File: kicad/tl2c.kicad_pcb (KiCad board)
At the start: 4 copper layers, 120.7 x 127 mm, 92 parts, among them IC101 ATTINY20-X, P101 12VDC, P102 I2C Master, P103 Spare, P104 ISP Header, P105 LED_DRIVER, P106 240VAC, P107 LED_DRIVER, P108 LED_OUT, P301 CONN_PIR_OG, P302 CONN_PIR_EG, P303 CONN_PIR_UG, Q301 IRLML2502, Q302 IRLML2502, Q303 IRLML2502, Q401 IRLML2502, Q402 IRLML2502, Q403 IRLML2502, SW101 TL3315NF160Q, U201 LF120ABDT-TR, U202 TPS70933

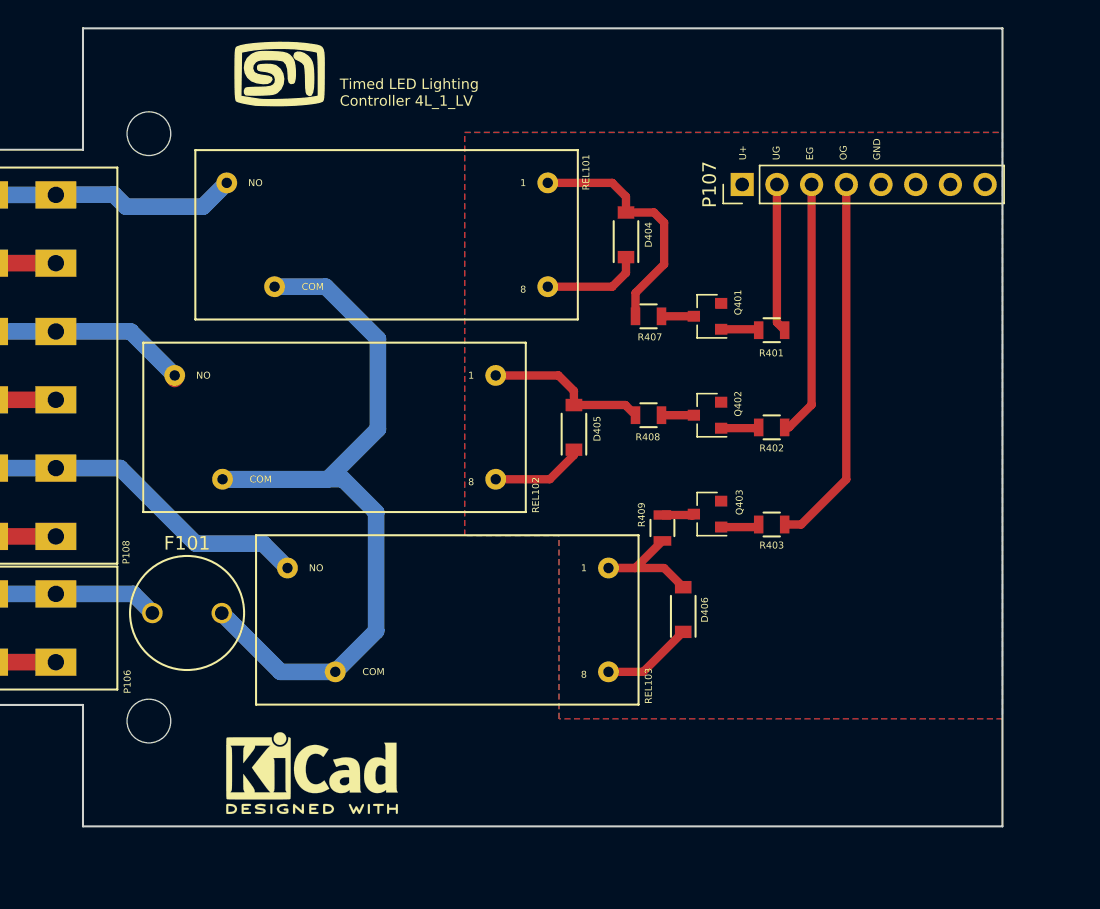
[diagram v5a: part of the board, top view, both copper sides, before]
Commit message: Created the Gerbers and submitted the order for boards and stensils
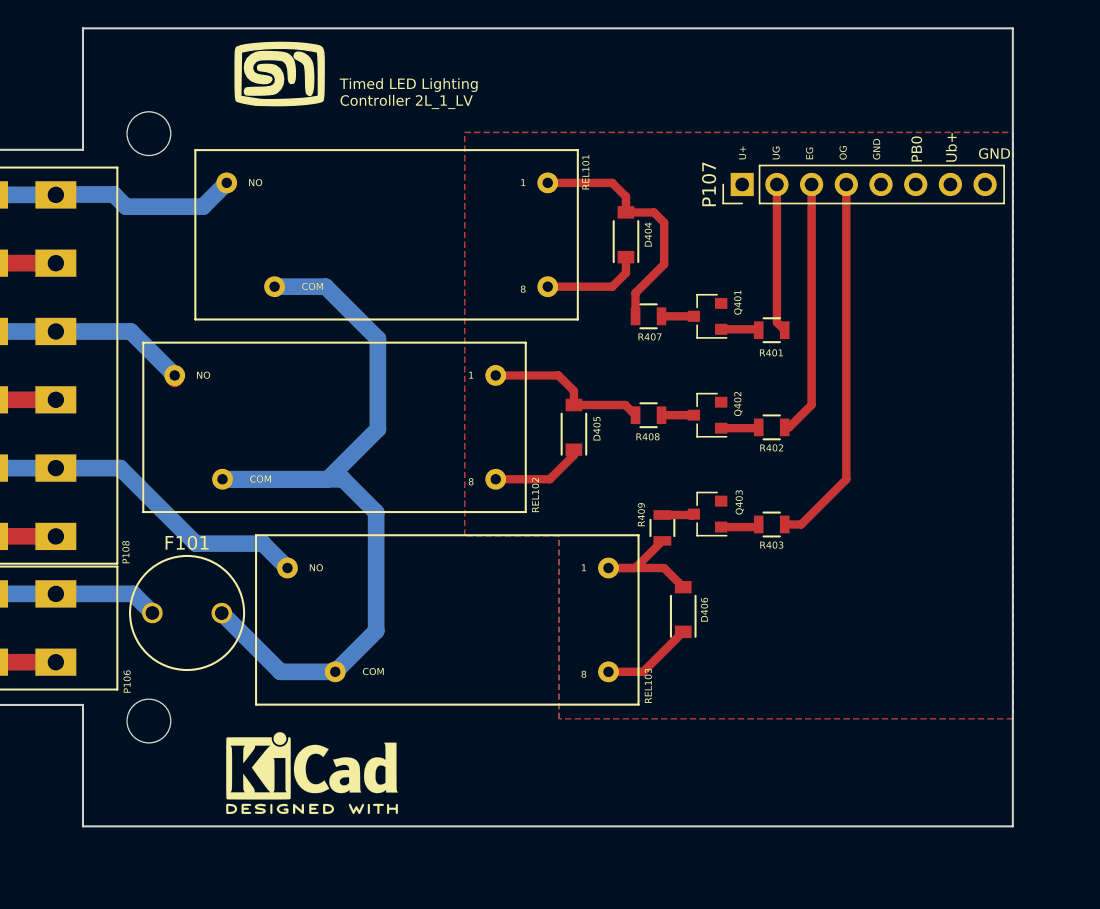
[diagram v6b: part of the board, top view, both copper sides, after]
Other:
- outline, holes or cut-outs redrawn
- board text added: "Timed LED Lighting Controller 2L_1_LV"
- board text removed: "Timed LED Lighting Controller 4L_1_LV"
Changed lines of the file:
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@@
     (area 11.304001 32.456 173.659715 192.505001)
     (thickness 1.6)
-    (drawings 108)
+    (drawings 111)
     (tracks 385)
     (zones 0)
@@
   )
   (setup
-    (last_trace_width 1.2192)
+    (last_trace_width 0.1524)
     (user_trace_width 0.3048)
     (user_trace_width 0.6096)
@@
     (pad_to_mask_clearance 0.2)
     (aux_axis_origin 0 0)
-    (visible_elements FFFEFFFF)
+    (visible_elements FFFEEFFF)
     (pcbplotparams
       (layerselection 0x010fc_80000007)
@@
       (net 52 /GPIO_PB0))
   )
+  (gr_text GND (at 113.792 61.2648) (layer F.SilkS)
+    (effects (font (size 0.762 0.762) (thickness 0.127)) (justify left))
+  )
+  (gr_text PB0 (at 109.3216 61.9252 90) (layer F.SilkS)
+    (effects (font (size 0.762 0.762) (thickness 0.127)) (justify left))
+  )
+  (gr_text Ub+ (at 111.8616 61.9252 90) (layer F.SilkS)
+    (effects (font (size 0.762 0.762) (thickness 0.127)) (justify left))
+  )
   (gr_text Ub+ (at 111.7346 130.4544 90) (layer F.SilkS)
     (effects (font (size 0.762 0.762) (thickness 0.127)) (justify left))
@@
     (effects (font (size 0.762 0.762) (thickness 0.127)) (justify left))
   )
-  (gr_text "Timed LED Lighting \nController 4L_1_LV" (at 67.056 56.769) (layer F.SilkS)
+  (gr_text "Timed LED Lighting \nController 2L_1_LV" (at 67.056 56.769) (layer F.SilkS)
     (effects (font (size 0.762 0.762) (thickness 0.127)) (justify left))
   )
@@
   (gr_line (start 92.71 120.65) (end 143.912 120.65) (angle 90) (layer Edge.Cuts) (width 0.15))
   (gr_line (start 48.26 60.96) (end 48.26 52.07) (angle 90) (layer Edge.Cuts) (width 0.15))
-  (gr_line (start 115.57 110.49) (end 48.26 110.49) (angle 90) (layer Edge.Cuts) (width 0.15))
-  (gr_line (start 115.57 52.07) (end 115.57 110.49) (angle 90) (layer Edge.Cuts) (width 0.15))
-  (gr_line (start 48.26 52.07) (end 115.57 52.07) (angle 90) (layer Edge.Cuts) (width 0.15))
+  (gr_line (start 116.332 110.49) (end 48.26 110.49) (angle 90) (layer Edge.Cuts) (width 0.15))
+  (gr_line (start 116.332 52.07) (end 116.332 110.49) (angle 90) (layer Edge.Cuts) (width 0.15))
+  (gr_line (start 48.26 52.07) (end 116.332 52.07) (angle 90) (layer Edge.Cuts) (width 0.15))
   (segment (start 102.886 169.799) (end 102.886 167.624) (width 1.2192) (layer F.Cu) (net 2))
   (segment (start 102.886 167.624) (end 105.918 164.592) (width 1.2192) (layer F.Cu) (net 2))
@@
   (segment (start 51.943 93.472) (end 53.34 94.869) (width 1.2192) (layer B.Cu) (net 17))
   (segment (start 41.275 93.472) (end 46.275 93.472) (width 1.2192) (layer B.Cu) (net 17))
-  (segment (start 46.275 64.262) (end 46.3004 64.2366) (width 1.2192) (layer B.Cu) (net 18) (status C00000))
-  (segment (start 46.3004 64.2366) (end 50.5206 64.2366) (width 1.2192) (layer B.Cu) (net 18) (status 400000))
-  (segment (start 57.0424 65.1256) (end 58.785 63.383) (width 1.2192) (layer B.Cu) (net 18) (status 800000))
+  (segment (start 46.275 64.262) (end 46.3004 64.2366) (width 1.2192) (layer B.Cu) (net 18))
+  (segment (start 46.3004 64.2366) (end 50.5206 64.2366) (width 1.2192) (layer B.Cu) (net 18))
+  (segment (start 57.0424 65.1256) (end 58.785 63.383) (width 1.2192) (layer B.Cu) (net 18))
   (segment (start 51.4096 65.1256) (end 57.0424 65.1256) (width 1.2192) (layer B.Cu) (net 18))
   (segment (start 50.5206 64.2366) (end 51.4096 65.1256) (width 1.2192) (layer B.Cu) (net 18))
@@
     (polygon
       (pts
-        (xy 83.1088 89.2048) (xy 76.2 89.2048) (xy 76.2 59.69) (xy 115.57 59.69) (xy 115.57 102.616)
+        (xy 83.1088 89.2048) (xy 76.2 89.2048) (xy 76.2 59.69) (xy 116.332 59.69) (xy 116.332 102.616)
         (xy 83.1088 102.616)
       )
@@
     (polygon
       (pts
-        (xy 115.57 102.616) (xy 83.1088 102.616) (xy 83.1088 89.2048) (xy 76.2 89.2048) (xy 76.2 59.69)
-        (xy 115.57 59.69) (xy 115.57 110.49)
+        (xy 116.332 102.616) (xy 83.1088 102.616) (xy 83.1088 89.2048) (xy 76.2 89.2048) (xy 76.2 59.69)
+        (xy 116.332 59.69)
       )
     )

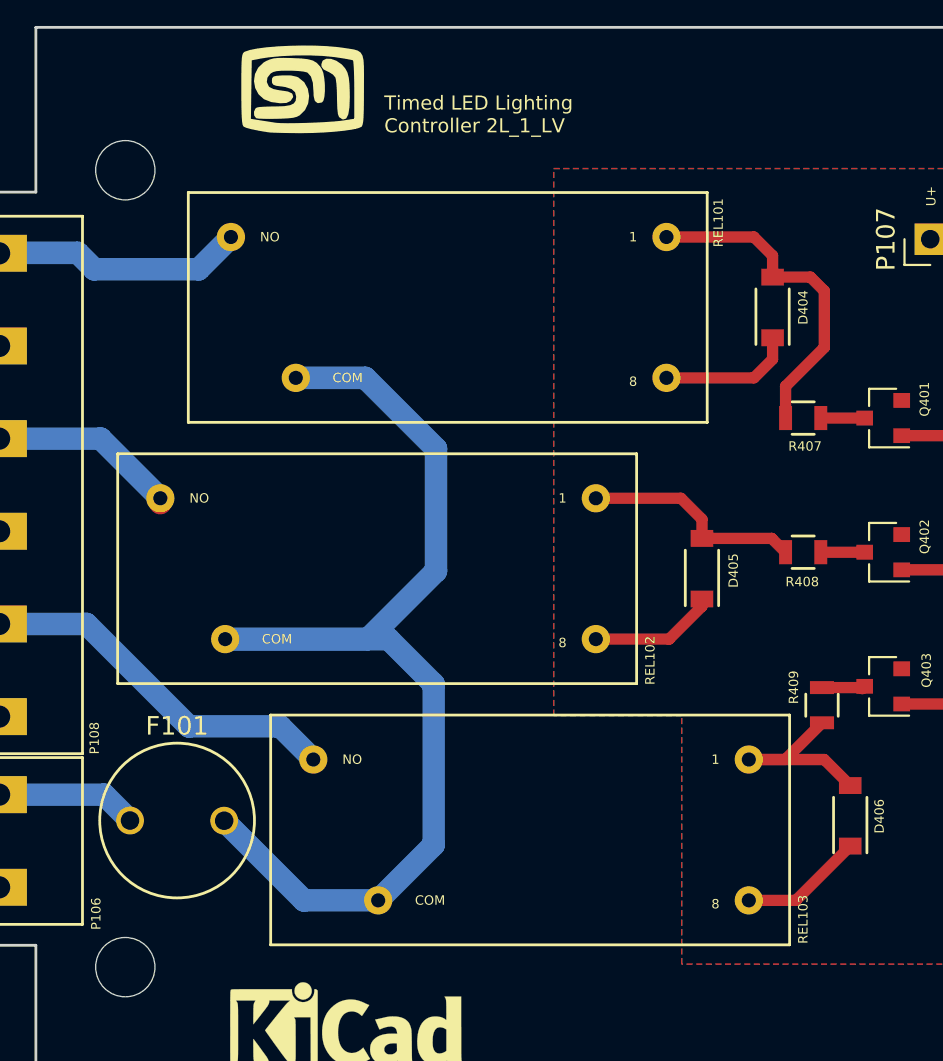
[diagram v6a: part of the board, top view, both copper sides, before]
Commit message: Updated the footprint for the relay - larger holes
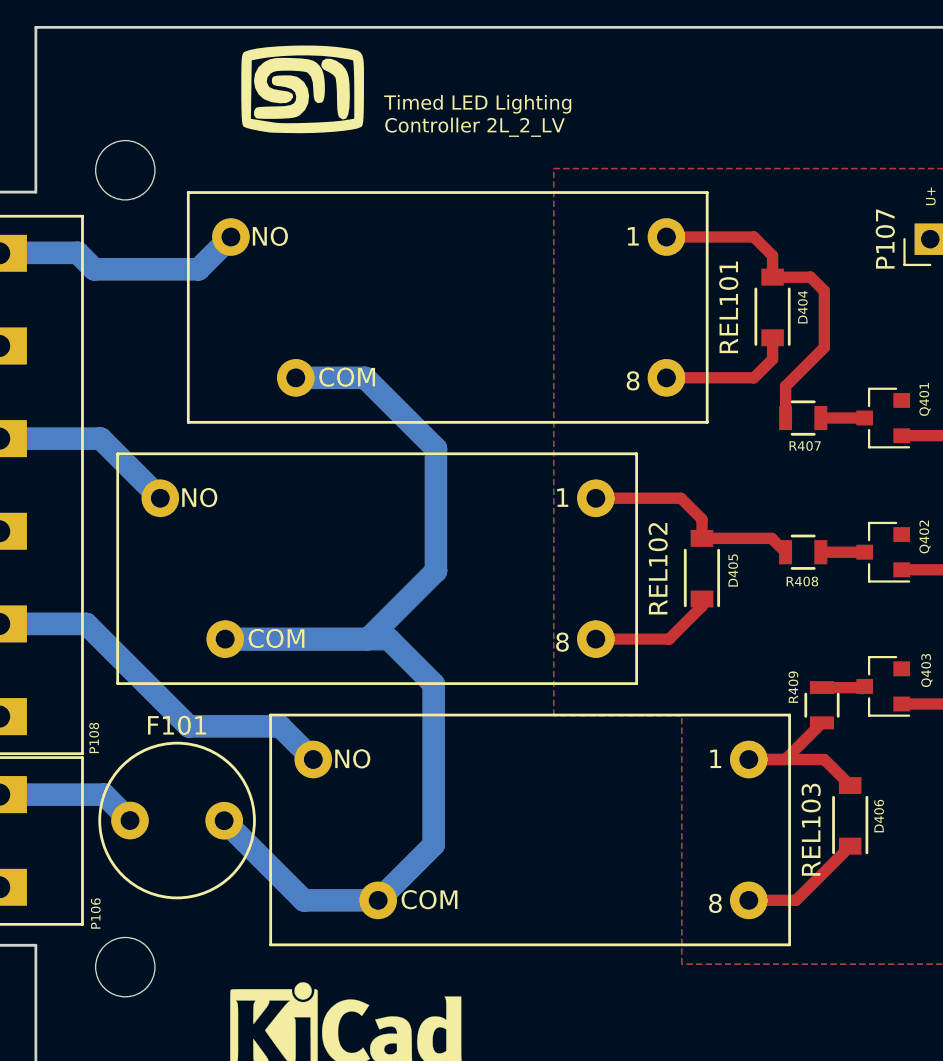
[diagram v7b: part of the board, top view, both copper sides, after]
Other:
- board text added: "Timed LED Lighting Controller 2L_2_LV"
- board text removed: "Timed LED Lighting Controller 2L_1_LV"
